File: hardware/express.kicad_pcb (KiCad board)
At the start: 4 copper layers, 180 x 35 mm, 180 parts, among them J1001 SJ2-25404B-SMT-TR, J101 Cortex_Debug, J1101 SJ2-25404B-SMT-TR, J1201 SJ2-25404B-SMT-TR, J1301 SJ2-25404B-SMT-TR, J1401 SJ2-25404B-SMT-TR, J1501 SJ2-25404B-SMT-TR, J1601 SJ2-25404B-SMT-TR, J1701 SJ2-25404B-SMT-TR, J1801 2x05_Horizontal, J1901 2x05_Horizontal, J201 SJ2-25404B-SMT-TR, J301 SJ2-25404B-SMT-TR, J401 SJ2-25404B-SMT-TR, J501 SJ2-25404B-SMT-TR, J601 SJ2-25404B-SMT-TR, J701 SJ2-25404B-SMT-TR, J801 SJ2-25404B-SMT-TR, J901 SJ2-25404B-SMT-TR, SW101 SW_Push, SW102 SW_Push, U101 TPS78433QWDRBRQ1, U102 ATSAMD51J, U1801 THVD24x2, U1901 THVD24x2, Y101 32k768

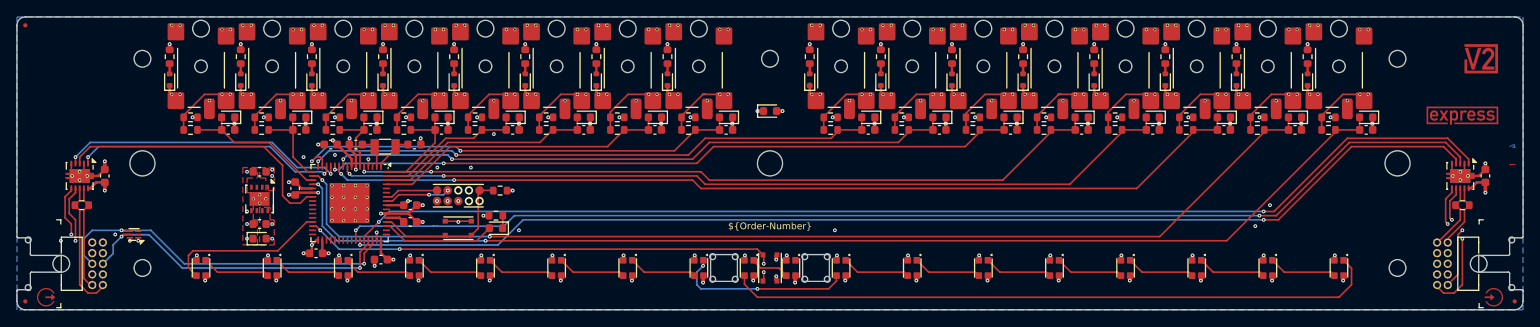
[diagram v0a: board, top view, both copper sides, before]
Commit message: Replace Order_Number
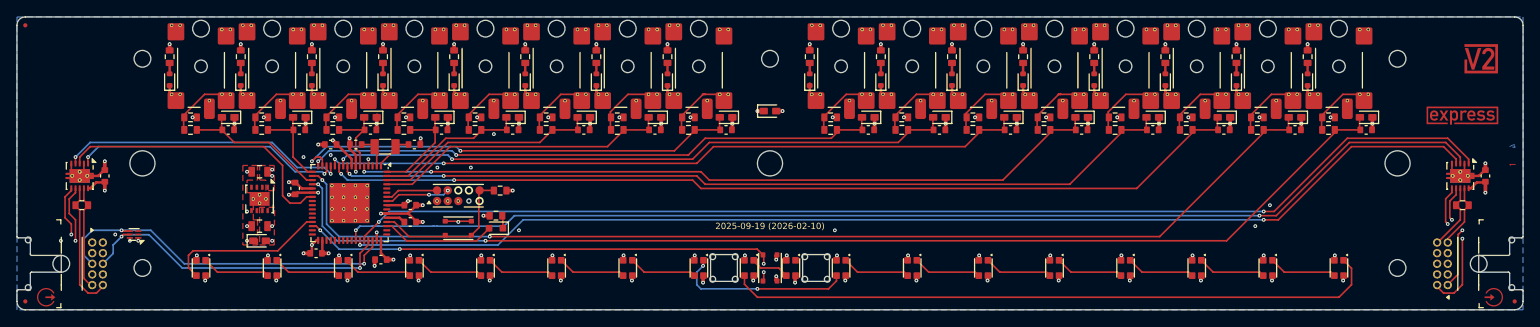
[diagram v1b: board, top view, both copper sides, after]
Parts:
- C1001, C101, C103, C104, C105, C106, C107, C110, C1101, C111, C1201, C1301, C1401, C1501, C1601, C1701, C1801, C1901, C201, C301, C401, C501, C601, C701, C801, C901: footprint Capacitor_SMD:C_0603_1608Metric -> V2_Capacitor_SMD:C_0603
- C108, C109: footprint Capacitor_SMD:C_0603_1608Metric -> V2_Capacitor_SMD:C_0805
- D1001, D1101, D1201, D1301, D1401, D1501, D1601, D1701, D201, D301, D401, D501, D601, D701, D801, D901: footprint Diode_SMD:D_SOD-523 -> V2_Diode_SMD:D_SOD-523
- D103: footprint LED_SMD:LED_0603_1608Metric -> V2_LED:LED_0603
- FID101, FID102, FID103: value Fiducial -> Fiducial_Paste
- H101, H102, H105: value MountingHole_3mm -> 3mm
- H103, H104, H106, H107, H108: value MountingHole_2mm -> 2mm
- INFO101: value Order_Number -> ~; footprint V2_Production:Order_Number -> V2_Production:Revision
- J101: value Cortex_Debug -> Cortex; footprint V2_Cortex_Debug:Cortex_Debug_Pad -> V2_Connector_Debug:Cortex
- R1001, R1002, R1003, R101, R102, R1101, R1102, R1103, R1201, R1202, R1203, R1301, R1302, R1303, R1401, R1402, R1403, R1501, R1502, R1503, R1601, R1602, R1603, R1701, R1702, R1703, R1801, R1901, R201, R202, R203, R301, R302, R303, R401, R402, R403, R501, R502, R503, R601, R602, R603, R701, R702, R703, R801, R802, R803, R901, R902, R903: footprint Resistor_SMD:R_0603_1608Metric -> V2_Resistor_SMD:R_0603
- SW101, SW102: value SW_Push -> SKSG
- TVS1001, TVS101, TVS102, TVS1101, TVS1201, TVS1301, TVS1401, TVS1501, TVS1601, TVS1701, TVS201, TVS301, TVS401, TVS501, TVS601, TVS701, TVS801, TVS901: footprint Diode_SMD:D_0603_1608Metric -> V2_Diode_SMD:D_0603
- U1801, U1901: value THVD24x2 -> THVD2442
- moved C108 0.25 mm to (91.5, 109.8)
- moved TVS101 0.25 mm to (91.5, 111.5)
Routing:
- net GND: track 85.5 -> 85.7 mm, vias 88 -> 86
- net +3V3: vias 29 -> 28

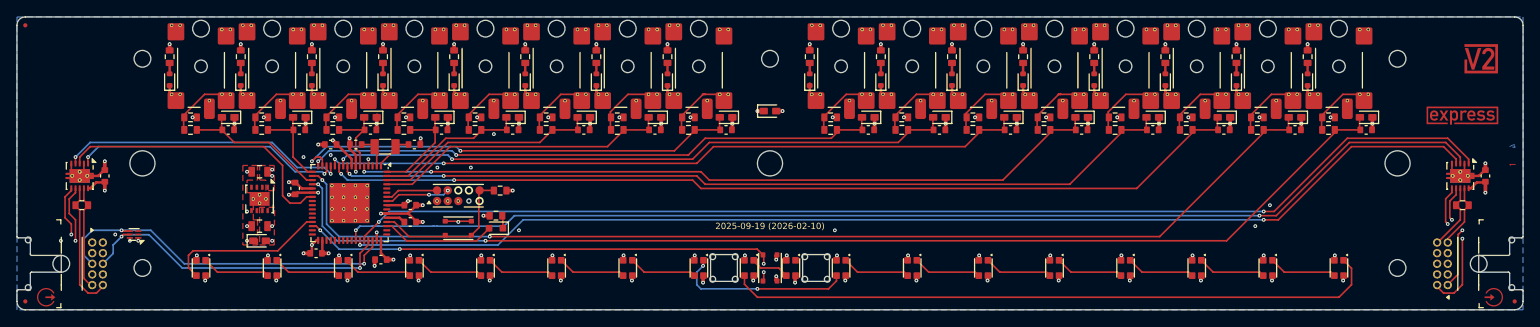
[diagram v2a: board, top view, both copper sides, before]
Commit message: Update ESD suppressor
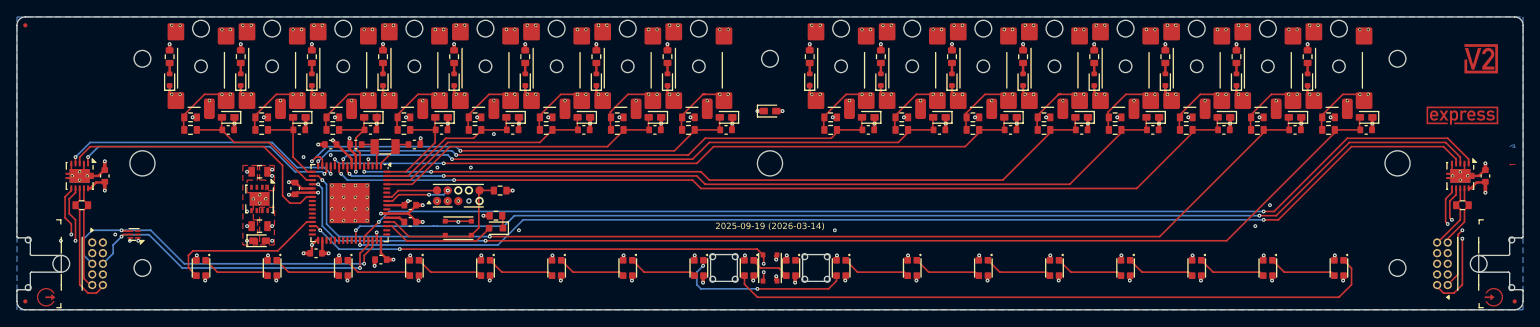
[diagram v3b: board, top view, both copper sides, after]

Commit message: Replace diode
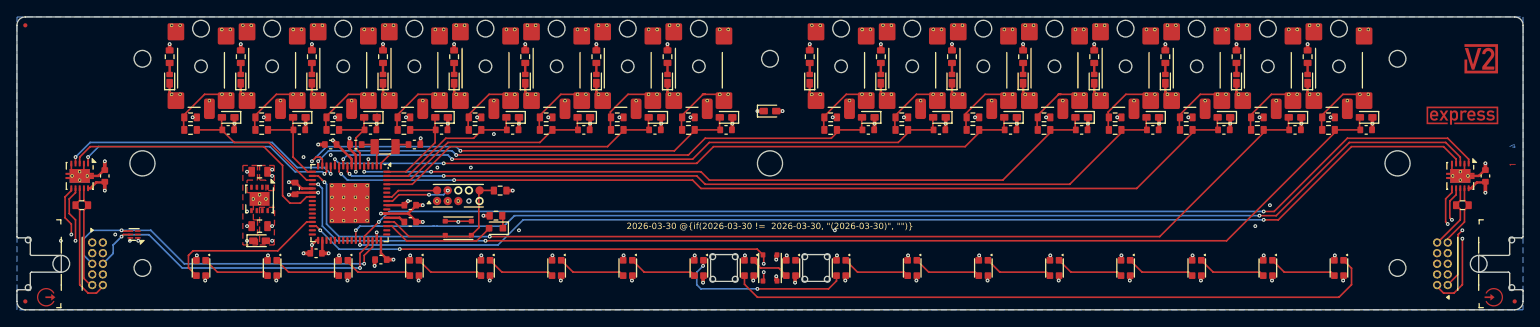
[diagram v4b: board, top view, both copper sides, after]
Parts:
- D1001, D1101, D1201, D1301, D1401, D1501, D1601, D1701, D201, D301, D401, D501, D601, D701, D801, D901: value RB501SM -> PMEG2010EPK; footprint V2_Diode_SMD:D_SOD-523 -> V2_Diode_SMD:D_SOD-1608
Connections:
- net / Expression Input 1/LED-Out renamed /Expression Input 1/LED-Out
- net / Expression Input 1/Ring renamed /Expression Input 1/Ring
- net / Expression Input 1/Tip renamed /Expression Input 1/Tip
- net / Expression Input 10/LED-In renamed /Expression Input 10/LED-In
- net / Expression Input 10/LED-Out renamed /Expression Input 10/LED-Out
- net / Expression Input 10/Ring renamed /Expression Input 10/Ring
- net / Expression Input 10/Tip renamed /Expression Input 10/Tip
- net / Expression Input 11/LED-Out renamed /Expression Input 11/LED-Out
- net / Expression Input 11/Ring renamed /Expression Input 11/Ring
- net / Expression Input 11/Tip renamed /Expression Input 11/Tip
- net / Expression Input 12/Ring renamed /Expression Input 12/Ring
- net / Expression Input 12/Tip renamed /Expression Input 12/Tip
- net / Expression Input 13/LED-Out renamed /Expression Input 13/LED-Out
- net / Expression Input 13/Ring renamed /Expression Input 13/Ring
- net / Expression Input 13/Tip renamed /Expression Input 13/Tip
- net / Expression Input 14/LED-Out renamed /Expression Input 14/LED-Out
- net / Expression Input 14/Ring renamed /Expression Input 14/Ring
- net / Expression Input 14/Tip renamed /Expression Input 14/Tip
- net / Expression Input 15/LED-Out renamed /Expression Input 15/LED-Out
- net / Expression Input 15/Ring renamed /Expression Input 15/Ring
- net / Expression Input 15/Tip renamed /Expression Input 15/Tip
- net / Expression Input 16/Ring renamed /Expression Input 16/Ring
- net / Expression Input 16/Tip renamed /Expression Input 16/Tip
- net / Expression Input 2/LED-Out renamed /Expression Input 2/LED-Out
- net / Expression Input 2/Ring renamed /Expression Input 2/Ring
- net / Expression Input 2/Tip renamed /Expression Input 2/Tip
- net / Expression Input 3/LED-Out renamed /Expression Input 3/LED-Out
- net / Expression Input 3/Ring renamed /Expression Input 3/Ring
- net / Expression Input 3/Tip renamed /Expression Input 3/Tip
- net / Expression Input 4/Ring renamed /Expression Input 4/Ring
- net / Expression Input 4/Tip renamed /Expression Input 4/Tip
- net / Expression Input 5 /LED-Out renamed /Expression Input 5/LED-Out
- net / Expression Input 5 /Ring renamed /Expression Input 5/Ring
- net / Expression Input 5 /Tip renamed /Expression Input 5/Tip
- net / Expression Input 6/LED-Out renamed /Expression Input 6/LED-Out
- net / Expression Input 6/Ring renamed /Expression Input 6/Ring
- net / Expression Input 6/Tip renamed /Expression Input 6/Tip
- net / Expression Input 7/LED-Out renamed /Expression Input 7/LED-Out
- net / Expression Input 7/Ring renamed /Expression Input 7/Ring
- net / Expression Input 7/Tip renamed /Expression Input 7/Tip
- net / Expression Input 8/Ring renamed /Expression Input 8/Ring
- net / Expression Input 8/Tip renamed /Expression Input 8/Tip
- net / Expression Input 9/Ring renamed /Expression Input 9/Ring
- net / Expression Input 9/Tip renamed /Expression Input 9/Tip

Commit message: Update
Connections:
- net /VDDCORE renamed /+VDDCORE
